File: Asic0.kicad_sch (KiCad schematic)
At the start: 19 parts, among them U2 BM1370_mode1

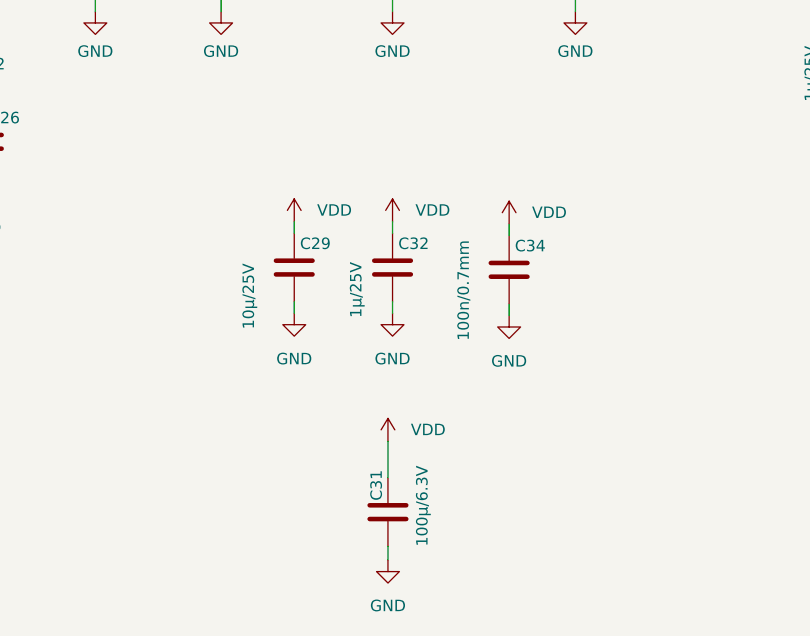
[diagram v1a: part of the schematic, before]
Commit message: board rev 3.0
- 6 phases using TPS53667
- Changed current MLCC capacitors to reduce BOM parts and rds on VRs
- Beads at LDOs, TDisplay, fans and Power input (EMC)
- Changed routing to allow better VDD circuit on bottom
- Reduced VDD area to avoid EMI
- New Layer distribution to reduce EMI
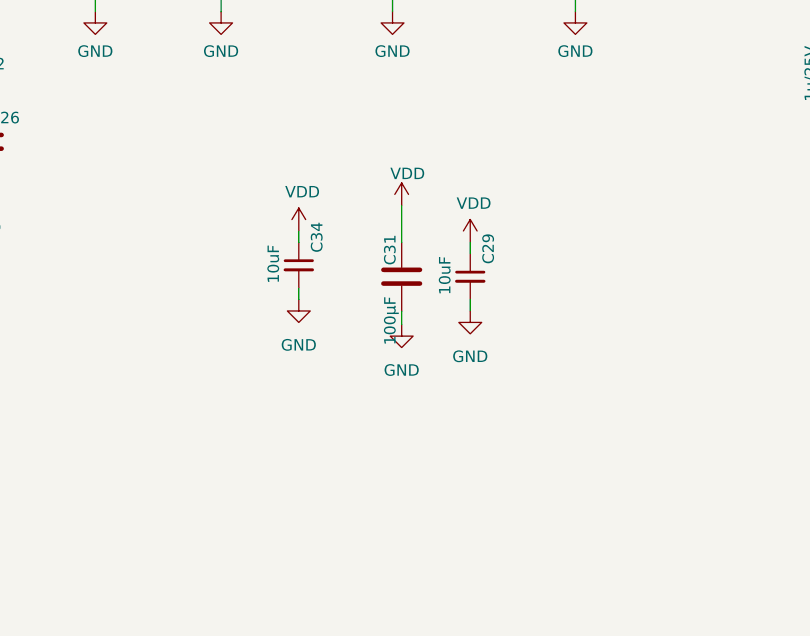
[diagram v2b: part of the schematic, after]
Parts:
- removed C29: 10µ/25V, Capacitor_SMD:C_0805_2012Metric, symbol Device:C
- removed C32: 1µ/25V, Capacitor_SMD:C_0805_2012Metric, symbol Device:C
- removed C34: 100n/0.7mm, Capacitor_SMD:C_0805_2012Metric, symbol Device:C
- added C29, C34: 10uF, Capacitor_SMD:C_0603_1608Metric, symbol Device:C_Small
- C31: value 100µ/6.3V -> 100µF; footprint Capacitor_SMD:C_1210_3225Metric -> Capacitor_SMD:C_1206_3216Metric; Brand KEMET -> (none); LCSC (none) -> C15008; Manufacturer C1210C107M8PAC7800 -> (none); Manufacturer  (none) -> Samsung Electro-Mechanics; PARTNO (none) -> CL31A107MQHNNNE; Size 1210 -> (none)
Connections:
- net GND: now also C29.2, C34.2
- net VDD: now also C29.1, C34.1

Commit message: Refactored buck stage and improved EMI performance
I've made several changes that I’d like to explain. Not sure yet if all of them are optimal, but they reflect my impressions and should help in several areas.

- Increased buck converter from 4 to 6 phases (now using TPS53667 controller).
- Changed layer stack to keep GND between VDD planes (to improve EMI).
- Added EMI filters at input, power beads, and additional ferrite beads in the 3V3 and 5V sections.
- Relocated the 5V LDO to optimize space in the regulator area.
- Standardized some input capacitors in the buck regulator stage.
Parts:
- C15, C17, C26, C27, C28, C30, C33, C35, C36, C37, C38, C40: LCSC (none) -> C116352
- C29, C34: LCSC C92487 Hot -> C92487
- R10: LCSC (none) -> C140868
- R9: LCSC (none) -> C17513
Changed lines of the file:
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@@
 			)
 		)
+		(property "LCSC" "C17513"
+			(at 104.394 86.106 90)
+			(effects
+				(font
+					(size 1.27 1.27)
+				)
+				(hide yes)
+			)
+		)
 		(pin "1"
 		)
@@
 			)
 		)
+		(property "LCSC" "C116352"
+			(at 91.948 112.014 0)
+			(effects
+				(font
+					(size 1.27 1.27)
+				)
+				(hide yes)
+			)
+		)
 		(pin "1"
 		)
@@
 			)
 		)
+		(property "LCSC" "C116352"
+			(at 162.814 42.926 90)
+			(effects
+				(font
+					(size 1.27 1.27)
+				)
+				(hide yes)
+			)
+		)
 		(pin "1"
 		)
@@
 			)
 		)
+		(property "LCSC" "C116352"
+			(at 175.514 42.926 90)
+			(effects
+				(font
+					(size 1.27 1.27)
+				)
+				(hide yes)
+			)
+		)
 		(pin "1"
 		)
@@
 			)
 		)
+		(property "LCSC" "C140868"
+			(at 174.244 78.486 90)
+			(effects
+				(font
+					(size 1.27 1.27)
+				)
+				(hide yes)
+			)
+		)
 		(pin "1"
 		)
@@
 			)
 		)
+		(property "LCSC" "C116352"
+			(at 186.944 42.926 90)
+			(effects
+				(font
+					(size 1.27 1.27)
+				)
+				(hide yes)
+			)
+		)
 		(pin "1"
 		)
@@
 			)
 		)
-		(property "LCSC" "C92487 Hot "
+		(property "LCSC" "C92487"
 			(at 127 125.73 0)
 			(effects
@@
 			)
 		)
+		(property "LCSC" "C116352"
+			(at 78.74 112.522 0)
+			(effects
+				(font
+					(size 1.27 1.27)
+				)
+				(hide yes)
+			)
+		)
 		(pin "1"
 		)
@@
 			)
 		)
+		(property "LCSC" "C116352"
+			(at 187.452 105.156 0)
+			(effects
+				(font
+					(size 1.27 1.27)
+				)
+				(hide yes)
+			)
+		)
 		(pin "1"
 		)
@@
 			)
 		)
+		(property "LCSC" "C116352"
+			(at 100.584 42.926 90)
+			(effects
+				(font
+					(size 1.27 1.27)
+				)
+				(hide yes)
+			)
+		)
 		(pin "1"
 		)
@@
 			)
 		)
+		(property "LCSC" "C116352"
+			(at 89.154 42.926 90)
+			(effects
+				(font
+					(size 1.27 1.27)
+				)
+				(hide yes)
+			)
+		)
 		(pin "1"
 		)
@@
 			)
 		)
-		(property "LCSC" "C92487 Hot "
+		(property "LCSC" "C92487"
 			(at 146.05 127 0)
 			(effects
@@
 			)
 		)
+		(property "LCSC" "C116352"
+			(at 148.844 42.926 90)
+			(effects
+				(font
+					(size 1.27 1.27)
+				)
+				(hide yes)
+			)
+		)
 		(pin "1"
 		)
@@
 			)
 		)
+		(property "LCSC" "C116352"
+			(at 112.014 42.926 90)
+			(effects
+				(font
+					(size 1.27 1.27)
+				)
+				(hide yes)
+			)
+		)
 		(pin "1"
 		)
@@
 			)
 		)
+		(property "LCSC" "C116352"
+			(at 200.152 104.902 0)
+			(effects
+				(font
+					(size 1.27 1.27)
+				)
+				(hide yes)
+			)
+		)
 		(pin "1"
 		)
@@
 			(effects
 				(font
+					(size 1.27 1.27)
+				)
+				(hide yes)
+			)
+		)
+		(property "LCSC" "C116352"
+			(at 128.524 42.926 90)
+			(effects
+				(font

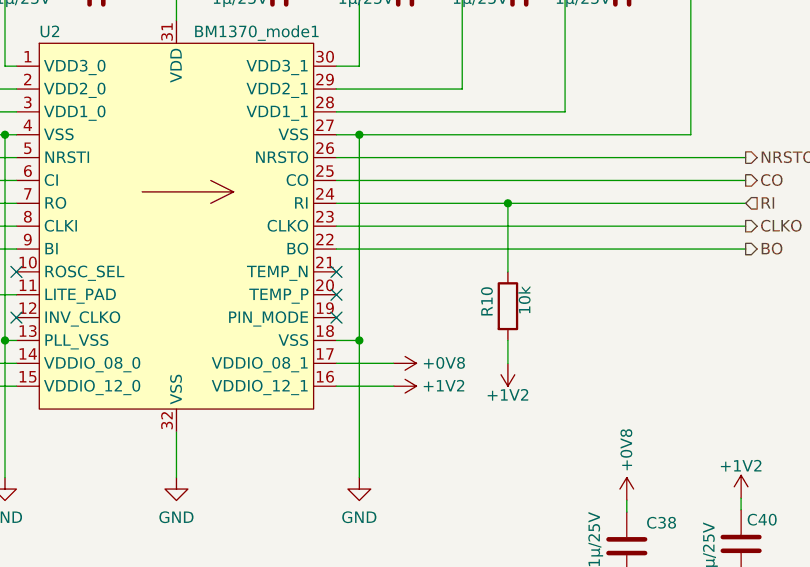
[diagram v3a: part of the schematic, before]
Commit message: Added TMP451 to schematic
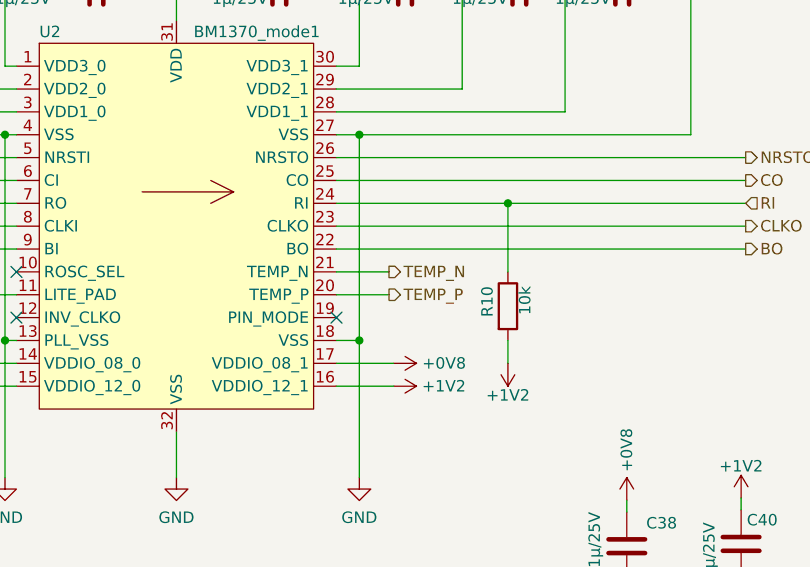
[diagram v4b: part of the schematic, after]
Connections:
- net TEMP_P: now reaches U2.20 (TEMP_P)
- net TEMP_N: now reaches U2.21 (TEMP_N)
- no-connect marks 5 -> 3
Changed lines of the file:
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@@
-	)
-	(no_connect
-		(at 155.194 74.676)
-	)
-	(no_connect
-		(at 155.194 77.216)
 	)
 	(no_connect
@@
 	(wire
 		(pts
+			(xy 155.194 77.216) (xy 161.036 77.216)
+		)
+		(stroke
+			(width 0)
+			(type default)
+		)
+	)
+	(wire
+		(pts
 			(xy 155.194 56.896) (xy 180.594 56.896)
 		)
@@
 		(pts
 			(xy 174.244 67.056) (xy 174.244 74.676)
+		)
+		(stroke
+			(width 0)
+			(type default)
+		)
+	)
+	(wire
+		(pts
+			(xy 155.194 74.676) (xy 161.036 74.676)
 		)
 		(stroke
@@
 		)
 	)
+	(hierarchical_label "TEMP_N"
+		(shape output)
+		(at 161.036 74.676 0)
+		(effects
+			(font
+				(size 1.27 1.27)
+			)
+			(justify left)
+		)
+	)
 	(hierarchical_label "CI"
 		(shape input)
@@
 		)
 	)
+	(hierarchical_label "TEMP_P"
+		(shape output)
+		(at 161.036 77.216 0)
+		(effects
+			(font
+				(size 1.27 1.27)
+			)
+			(justify left)
+		)
+	)

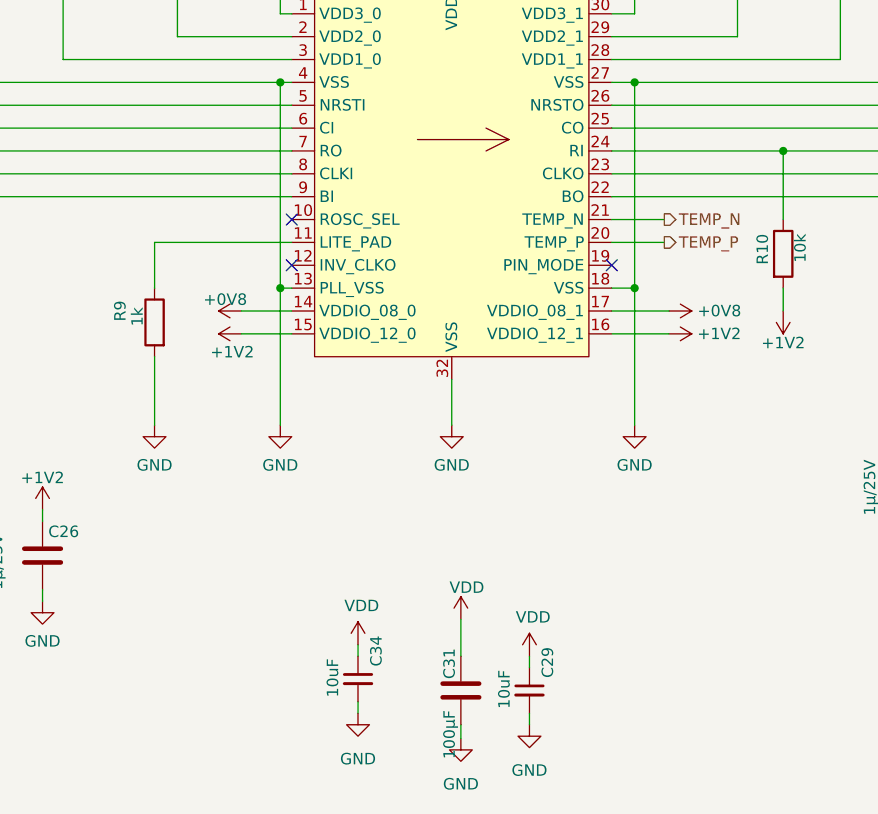
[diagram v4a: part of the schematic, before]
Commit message: Corrected Partnumbers (DK)
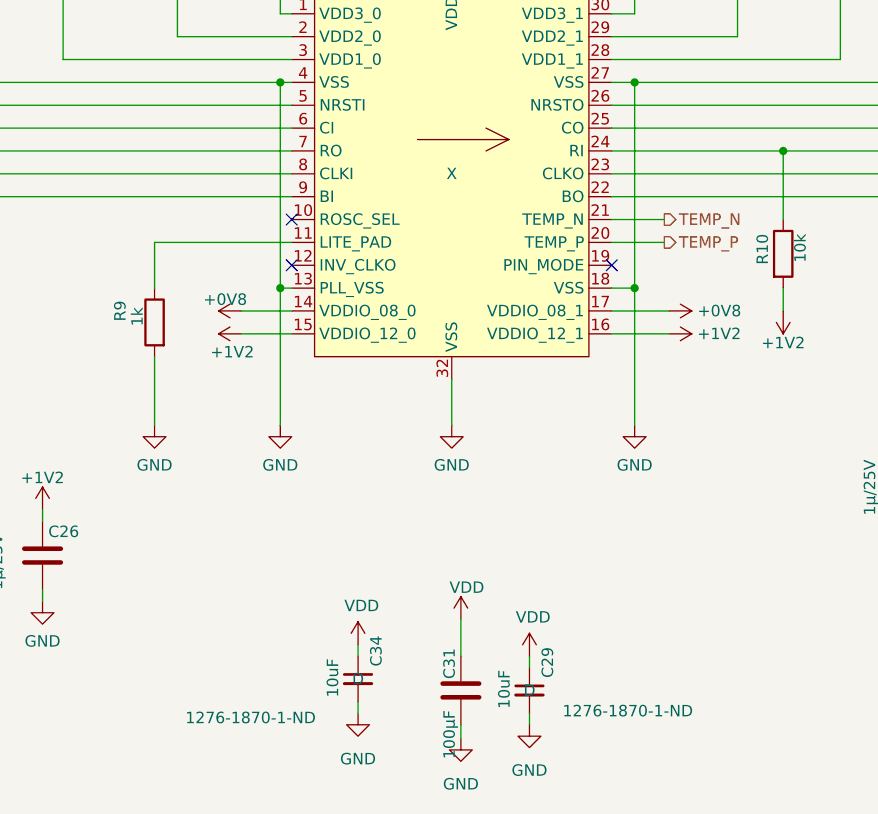
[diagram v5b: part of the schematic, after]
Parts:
- C29, C34: Distributor (none) -> D; OrderNr (none) -> 1276-1870-1-ND
- U2: Distributor (none) -> X
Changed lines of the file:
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@@
+			)
+		)
+		(property "Distributor" "D"
+			(at 127 125.73 0)
+			(effects
+				(font
+					(size 1.27 1.27)
+				)
+			)
+		)
+		(property "OrderNr" "1276-1870-1-ND"
+			(at 115.062 130.048 0)
+			(effects
+				(font
+					(size 1.27 1.27)
+				)
 			)
 		)
@@
 			)
 		)
+		(property "Distributor" "X"
+			(at 137.414 69.596 0)
+			(effects
+				(font
+					(size 1.27 1.27)
+				)
+			)
+		)
 		(pin "10"
 		)
@@
 			)
 		)
+		(property "Distributor" "D"
+			(at 146.05 127 0)
+			(effects
+				(font
+					(size 1.27 1.27)
+				)
+			)
+		)
+		(property "OrderNr" "1276-1870-1-ND"
+			(at 156.972 129.286 0)
+			(effects
+				(font
+					(size 1.27 1.27)
+				)
+			)
+		)
